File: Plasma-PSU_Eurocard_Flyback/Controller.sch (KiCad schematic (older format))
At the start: 10 parts

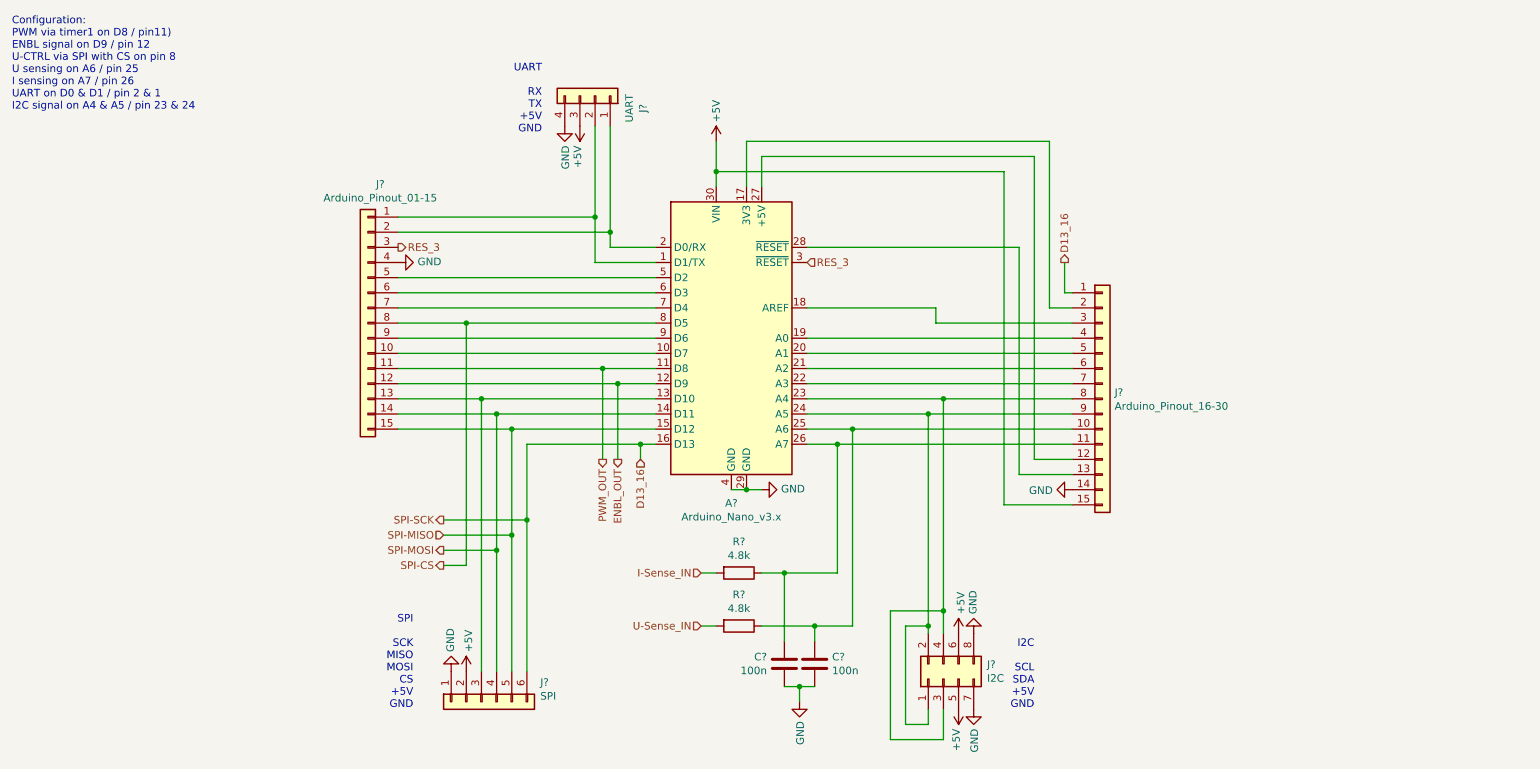
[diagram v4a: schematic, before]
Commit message: Footprints added
All footprints included, except:
- Boost Inductor
- 60A fuse holder
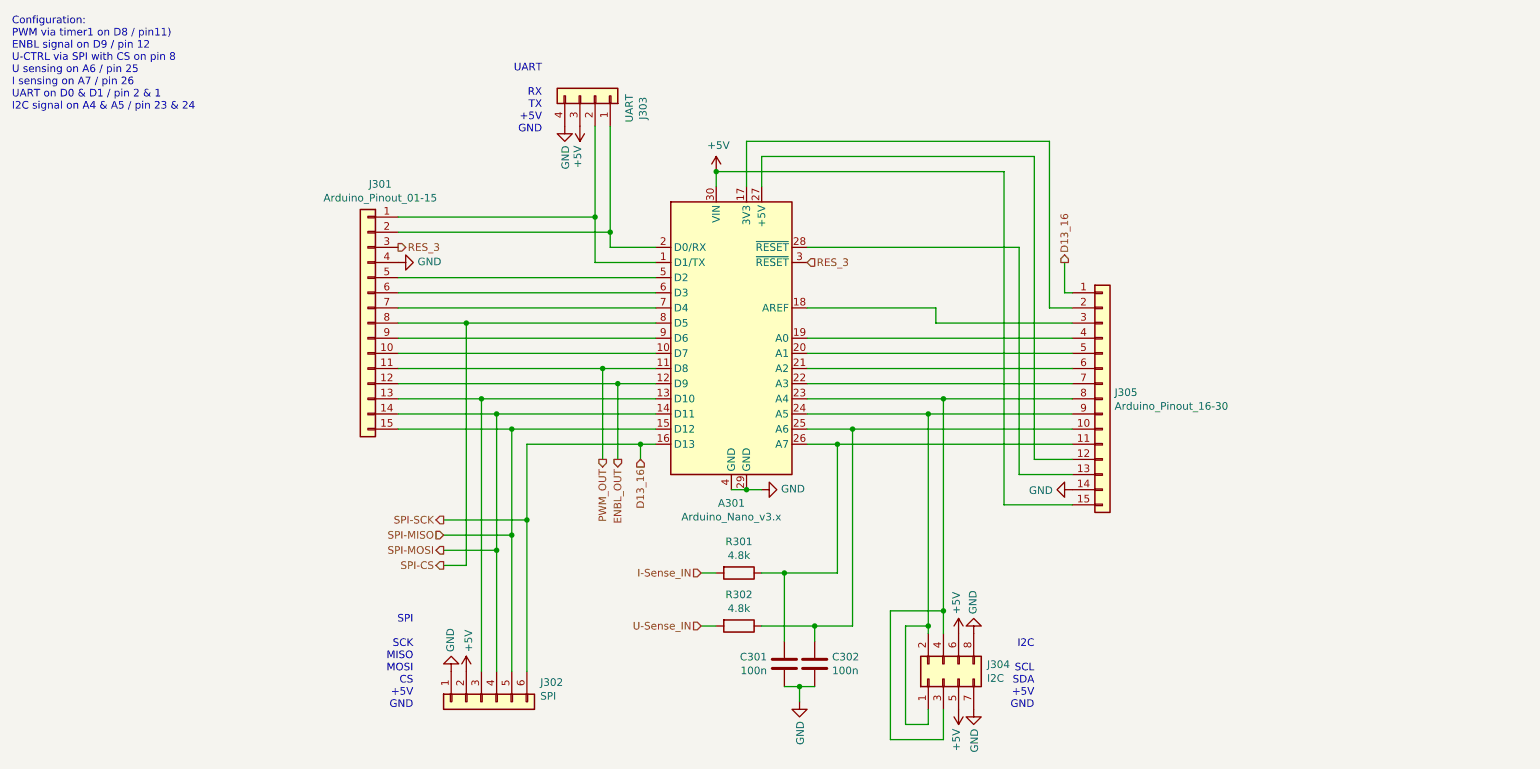
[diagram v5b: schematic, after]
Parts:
- C301, C302: renamed from C?; footprint (none) -> Capacitor_SMD:C_0201_0603Metric
- J301, J305: renamed from J?; footprint (none) -> Connector_PinHeader_2.54mm:PinHeader_1x15_P2.54mm_Vertical
- J302: renamed from J?; footprint (none) -> Connector_PinHeader_2.54mm:PinHeader_1x06_P2.54mm_Vertical
- J303: renamed from J?; footprint (none) -> Connector_PinHeader_2.54mm:PinHeader_1x04_P2.54mm_Vertical
- J304: renamed from J?; footprint (none) -> Connector_PinHeader_2.54mm:PinHeader_2x04_P2.54mm_Vertical
- R301, R302: renamed from R?; footprint (none) -> Resistor_THT:R_Axial_DIN0207_L6.3mm_D2.5mm_P7.62mm_Horizontal
- gave numbers to parts that had none: 1
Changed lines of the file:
@@
 $EndDescr
 $Comp
-L MCU_Module:Arduino_Nano_v3.x A?
+L MCU_Module:Arduino_Nano_v3.x A301
 U 1 1 5E8B3D3C
 P 5500 2800
-F 0 "A?" H 5500 1711 50  0000 C CNN
+F 0 "A301" H 5500 1711 50  0000 C CNN
 F 1 "Arduino_Nano_v3.x" H 5500 1620 50  0000 C CNN
 F 2 "Module:Arduino_Nano" H 5500 2800 50  0001 C CIN
@@
 U-Sense_IN
 $Comp
-L power:+5V #PWR?
-U 1 1 5E9350B4
-P 5400 1500
-F 0 "#PWR?" H 5400 1350 50  0001 C CNN
-F 1 "+5V" V 5400 1700 50  0000 C CNN
-F 2 "" H 5400 1500 50  0001 C CNN
-F 3 "" H 5400 1500 50  0001 C CNN
-	1    5400 1500
-	1    0    0    -1
-$EndComp
-$Comp
-L power:GND #PWR?
+L power:GND #PWR0153
 U 1 1 5E935810
 P 5700 3800
-F 0 "#PWR?" H 5700 3550 50  0001 C CNN
+F 0 "#PWR0153" H 5700 3550 50  0001 C CNN
 F 1 "GND" V 5705 3672 50  0000 R CNN
 F 2 "" H 5700 3800 50  0001 C CNN
@@
 Configuration:\nPWM via timer1 on D8 / pin11)\nENBL signal on D9 / pin 12\nU-CTRL via SPI with CS on pin 8\nU sensing on A6 / pin 25\nI sensing on A7 / pin 26\nUART on D0 & D1 / pin 2 & 1\nI2C signal on A4 & A5 / pin 23 & 24
 $Comp
-L Connector_Generic:Conn_01x04 J?
+L Connector_Generic:Conn_01x04 J303
 U 1 1 5E93DA08
 P 4600 1200
-F 0 "J?" H 4518 1517 50  0000 C CNN
+F 0 "J303" H 4518 1517 50  0000 C CNN
 F 1 "UART" H 4518 1426 50  0000 C CNN
-F 2 "" H 4600 1200 50  0001 C CNN
+F 2 "Connector_PinHeader_2.54mm:PinHeader_1x04_P2.54mm_Vertical" H 4600 1200 50  0001 C CNN
 F 3 "~" H 4600 1200 50  0001 C CNN
 	1    4600 1200
@@
 $EndComp
 $Comp
-L power:+5V #PWR?
+L power:+5V #PWR0154
 U 1 1 5E93EF11
 P 4500 1400
-F 0 "#PWR?" H 4500 1250 50  0001 C CNN
+F 0 "#PWR0154" H 4500 1250 50  0001 C CNN
 F 1 "+5V" V 4515 1528 50  0000 L CNN
 F 2 "" H 4500 1400 50  0001 C CNN
@@
 $EndComp
 $Comp
-L power:GND #PWR?
+L power:GND #PWR0155
 U 1 1 5E93F619
 P 4400 1400
-F 0 "#PWR?" H 4400 1150 50  0001 C CNN
+F 0 "#PWR0155" H 4400 1150 50  0001 C CNN
 F 1 "GND" V 4405 1272 50  0000 R CNN
 F 2 "" H 4400 1400 50  0001 C CNN
@@
 UART\n\nRX\nTX\n+5V\nGND
 $Comp
-L power:+5V #PWR?
-U 1 1 5E905601
-P 7000 4750
-F 0 "#PWR?" H 7000 4600 50  0001 C CNN
-F 1 "+5V" V 7015 4878 50  0000 L CNN
-F 2 "" H 7000 4750 50  0001 C CNN
-F 3 "" H 7000 4750 50  0001 C CNN
-	1    7000 4750
-	1    0    0    -1
-$EndComp
-$Comp
-L power:GND #PWR?
+L power:GND #PWR0157
 U 1 1 5E9057DA
 P 7100 4750
-F 0 "#PWR?" H 7100 4500 50  0001 C CNN
+F 0 "#PWR0157" H 7100 4500 50  0001 C CNN
 F 1 "GND" V 7105 4622 50  0000 R CNN
 F 2 "" H 7100 4750 50  0001 C CNN
@@
 $EndBitmap
 $Comp
-L Connector_Generic:Conn_01x15 J?
+L Connector_Generic:Conn_01x15 J301
 U 1 1 5EA28336
 P 3100 2700
-F 0 "J?" H 3018 3617 50  0000 C CNN
+F 0 "J301" H 3018 3617 50  0000 C CNN
 F 1 "Arduino_Pinout_01-15" H 3018 3526 50  0000 C CNN
-F 2 "" H 3100 2700 50  0001 C CNN
+F 2 "Connector_PinHeader_2.54mm:PinHeader_1x15_P2.54mm_Vertical" H 3100 2700 50  0001 C CNN
 F 3 "~" H 3100 2700 50  0001 C CNN
 	1    3100 2700
@@
 	4600 2300 5000 2300
 $Comp
-L power:GND #PWR?
+L power:GND #PWR0158
 U 1 1 5EA2DB7A
 P 3300 2300
-F 0 "#PWR?" H 3300 2050 50  0001 C CNN
+F 0 "#PWR0158" H 3300 2050 50  0001 C CNN
 F 1 "GND" V 3305 2172 50  0000 R CNN
 F 2 "" H 3300 2300 50  0001 C CNN
@@
 	4650 3000 5000 3000
 $Comp
-L Connector_Generic:Conn_01x15 J?
+L Connector_Generic:Conn_01x15 J305
 U 1 1 5EA3798C
 P 7950 3200
-F 0 "J?" H 8030 3242 50  0000 L CNN
+F 0 "J305" H 8030 3242 50  0000 L CNN
 F 1 "Arduino_Pinout_16-30" H 8030 3151 50  0000 L CNN
-F 2 "" H 7950 3200 50  0001 C CNN
+F 2 "Connector_PinHeader_2.54mm:PinHeader_1x15_P2.54mm_Vertical" H 7950 3200 50  0001 C CNN
 F 3 "~" H 7950 3200 50  0001 C CNN
 	1    7950 3200
@@
 	5600 1500 5600 1800
 Wire Wire Line
-	5400 1500 5400 1700
-Wire Wire Line
 	6850 2700 6850 2600
 Wire Wire Line
@@
 	7400 2200 6000 2200
 $Comp
-L power:GND #PWR?
+L power:GND #PWR0159
 U 1 1 5EA708AC
 P 7750 3800
-F 0 "#PWR?" H 7750 3550 50  0001 C CNN
+F 0 "#PWR0159" H 7750 3550 50  0001 C CNN
 F 1 "GND" V 7755 3672 50  0000 R CNN
 F 2 "" H 7750 3800 50  0001 C CNN
@@
 Wire Wire Line
 	7300 1700 5400 1700
-Connection ~ 5400 1700
 Wire Wire Line
 	5400 1700 5400 1800
@@
 I2C\n\nSCL\nSDA\n+5V\nGND
 $Comp
-L Connector_Generic:Conn_02x04_Odd_Even J?
+L Connector_Generic:Conn_02x04_Odd_Even J304
 U 1 1 5EA9327A
 P 6900 5050
-F 0 "J?" V 6996 4762 50  0000 R CNN
+F 0 "J304" V 6996 4762 50  0000 R CNN
 F 1 "I2C" V 6905 4762 50  0000 R CNN
-F 2 "" H 6900 5050 50  0001 C CNN
+F 2 "Connector_PinHeader_2.54mm:PinHeader_2x04_P2.54mm_Vertical" H 6900 5050 50  0001 C CNN
 F 3 "~" H 6900 5050 50  0001 C CNN
 	1    6900 5050
@@
 	6900 4600 6900 4750
 $Comp
-L power:+5V #PWR?
+L power:+5V #PWR0160
 U 1 1 5EA9EB31
 P 7000 5250
-F 0 "#PWR?" H 7000 5100 50  0001 C CNN
+F 0 "#PWR0160" H 7000 5100 50  0001 C CNN
 F 1 "+5V" V 7015 5378 50  0000 L CNN
 F 2 "" H 7000 5250 50  0001 C CNN
@@
 $EndComp
 $Comp
-L power:GND #PWR?
+L power:GND #PWR0161
 U 1 1 5EA9F288
 P 7100 5250
-F 0 "#PWR?" H 7100 5000 50  0001 C CNN
+F 0 "#PWR0161" H 7100 5000 50  0001 C CNN
 F 1 "GND" V 7105 5122 50  0000 R CNN
 F 2 "" H 7100 5250 50  0001 C CNN
@@
 Connection ~ 4900 3500
 $Comp
-L Device:R R?
+L Device:R R301
 U 1 1 5E90D904
 P 5550 4350
-F 0 "R?" V 5343 4350 50  0000 C CNN
+F 0 "R301" V 5343 4350 50  0000 C CNN
 F 1 "4.8k" V 5434 4350 50  0000 C CNN
-F 2 "" V 5480 4350 50  0001 C CNN
+F 2 "Resistor_THT:R_Axial_DIN0207_L6.3mm_D2.5mm_P7.62mm_Horizontal" V 5480 4350 50  0001 C CNN
 F 3 "~" H 5550 4350 50  0001 C CNN
 	1    5550 4350
@@
 $EndComp
 $Comp
-L Device:R R?
+L Device:R R302
 U 1 1 5E90DE41
 P 5550 4700
-F 0 "R?" V 5343 4700 50  0000 C CNN
+F 0 "R302" V 5343 4700 50  0000 C CNN
 F 1 "4.8k" V 5434 4700 50  0000 C CNN
-F 2 "" V 5480 4700 50  0001 C CNN
+F 2 "Resistor_THT:R_Axial_DIN0207_L6.3mm_D2.5mm_P7.62mm_Horizontal" V 5480 4700 50  0001 C CNN
 F 3 "~" H 5550 4700 50  0001 C CNN
 	1    5550 4700
@@
 	6300 3400 6300 4700
 $Comp
-L Device:C C?
+L Device:C C301
 U 1 1 5E9180BC
 P 5850 4950
-F 0 "C?" H 5735 4904 50  0000 R CNN
+F 0 "C301" H 5735 4904 50  0000 R CNN
 F 1 "100n" H 5735 4995 50  0000 R CNN
-F 2 "" H 5888 4800 50  0001 C CNN
+F 2 "Capacitor_SMD:C_0201_0603Metric" H 5888 4800 50  0001 C CNN
 F 3 "~" H 5850 4950 50  0001 C CNN
 	1    5850 4950
@@
 $EndComp
 $Comp
-L Device:C C?
+L Device:C C302
 U 1 1 5E9189A9
 P 6050 4950
-F 0 "C?" H 6165 4996 50  0000 L CNN
+F 0 "C302" H 6165 4996 50  0000 L CNN
 F 1 "100n" H 6165 4905 50  0000 L CNN
-F 2 "" H 6088 4800 50  0001 C CNN
+F 2 "Capacitor_SMD:C_0201_0603Metric" H 6088 4800 50  0001 C CNN
 F 3 "~" H 6050 4950 50  0001 C CNN
 	1    6050 4950
@@
 Wire Wire Line
 	6050 4800 6050 4700
-$Comp
-L power:GND #PWR?
-U 1 1 5E92882A
-P 5950 5200
-F 0 "#PWR?" H 5950 4950 50  0001 C CNN
-F 1 "GND" V 5955 5072 50  0000 R CNN
-F 2 "" H 5950 5200 50  0001 C CNN
-F 3 "" H 5950 5200 50  0001 C CNN
-	1    5950 5200
-	1    0    0    -1
-$EndComp
 Wire Wire Line
 	5850 5100 5950 5100
@@
 SPI\n\nSCK\nMISO\nMOSI\nCS\n+5V\nGND
 $Comp
-L power:+5V #PWR?
+L power:+5V #PWR0163
 U 1 1 5EA927CA
 P 3750 5000
-F 0 "#PWR?" H 3750 4850 50  0001 C CNN
+F 0 "#PWR0163" H 3750 4850 50  0001 C CNN
 F 1 "+5V" V 3765 5128 50  0000 L CNN
 F 2 "" H 3750 5000 50  0001 C CNN
@@
 $EndComp
 $Comp
-L power:GND #PWR?
+L power:GND #PWR0164
 U 1 1 5EA92261
 P 3650 5000
-F 0 "#PWR?" H 3650 4750 50  0001 C CNN
+F 0 "#PWR0164" H 3650 4750 50  0001 C CNN
 F 1 "GND" V 3655 4872 50  0000 R CNN
 F 2 "" H 3650 5000 50  0001 C CNN
@@
 $EndComp
 $Comp
-L Connector_Generic:Conn_01x06 J?
+L Connector_Generic:Conn_01x06 J302
 U 1 1 5EA74613
 P 3850 5200
-F 0 "J?" V 3722 4812 50  0000 R CNN
+F 0 "J302" V 3722 4812 50  0000 R CNN
 F 1 "SPI" V 3813 4812 50  0000 R CNN
-F 2 "" H 3850 5200 50  0001 C CNN
+F 2 "Connector_PinHeader_2.54mm:PinHeader_1x06_P2.54mm_Vertical" H 3850 5200 50  0001 C CNN
 F 3 "~" H 3850 5200 50  0001 C CNN
 	1    3850 5200
@@
 Wire Wire Line
 	6000 2800 7750 2800
+$Comp
+L power:+5V #PWR0156
+U 1 1 5E930D1E
+P 7000 4750
+F 0 "#PWR0156" H 7000 4600 50  0001 C CNN
+F 1 "+5V" V 7015 4878 50  0000 L CNN
+F 2 "" H 7000 4750 50  0001 C CNN
+F 3 "" H 7000 4750 50  0001 C CNN
+	1    7000 4750
+	-1   0    0    -1
+$EndComp
+$Comp
+L power:GND #PWR0162
+U 1 1 5E939308
+P 5950 5200
+F 0 "#PWR0162" H 5950 4950 50  0001 C CNN
+F 1 "GND" V 5955 5072 50  0000 R CNN
+F 2 "" H 5950 5200 50  0001 C CNN
+F 3 "" H 5950 5200 50  0001 C CNN
+	1    5950 5200
+	1    0    0    -1
+$EndComp
+$Comp
+L power:+5V #PWR0112
+U 1 1 5E9A5C22
+P 5400 1700
+F 0 "#PWR0112" H 5400 1550 50  0001 C CNN
+F 1 "+5V" H 5415 1873 50  0000 C CNN
+F 2 "" H 5400 1700 50  0001 C CNN
+F 3 "" H 5400 1700 50  0001 C CNN
+	1    5400 1700
+	1    0    0    -1
+$EndComp
+Connection ~ 5400 1700
 $EndSCHEMATC
